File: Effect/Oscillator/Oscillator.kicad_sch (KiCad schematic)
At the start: 19 parts, among them J1 Conn_01x04_Pin, J2 Conn_01x03_Pin, Q1 DMMT5401, Q2 DMMT5551, U1 OPA1655, U2 LM393

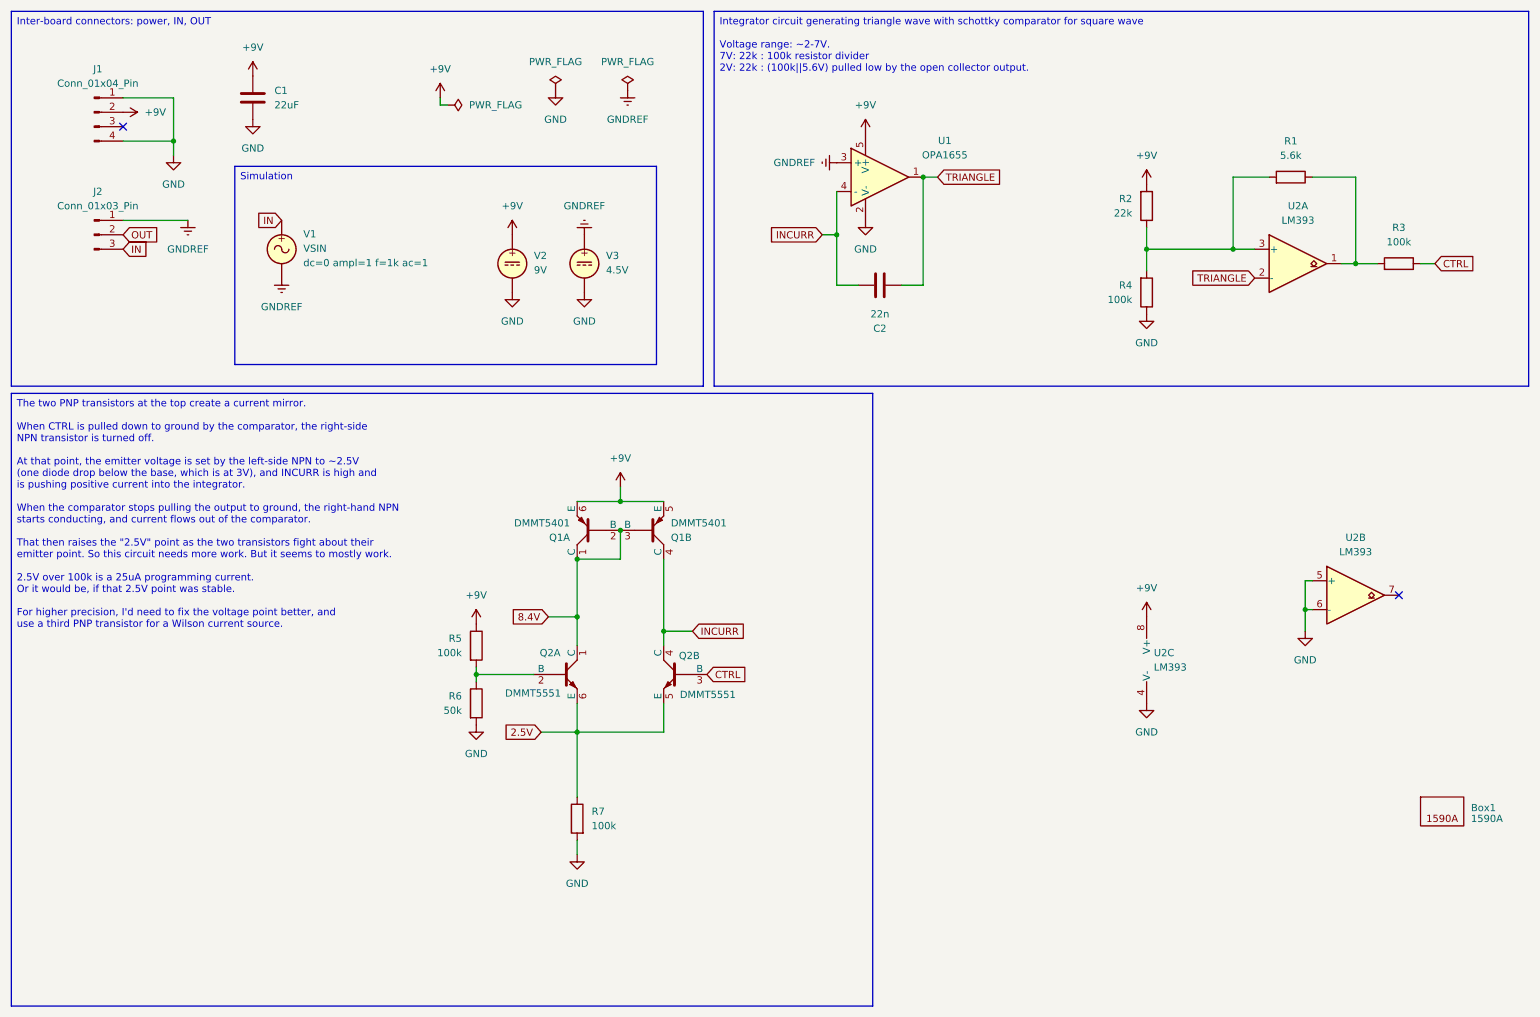
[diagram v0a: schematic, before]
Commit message: Connect up oscillator into a test board
Make a 'sineish' output by using a dual opamp and another integrator
circuit to turn the triangle wave into something that approximates a
sine wave.

It would be closer if my triangle wave was more balanced, but it looks
reasonable.  Even if the volume ends up being frequency dependent
because of how the integrator works - I haven't figured out how to fix
that part up.

Now it's an "effects pedal" with no inputs, only an output.  Simplest
way to test it.

Signed-off-by: Linus Torvalds <torvalds@linux-foundation.org>
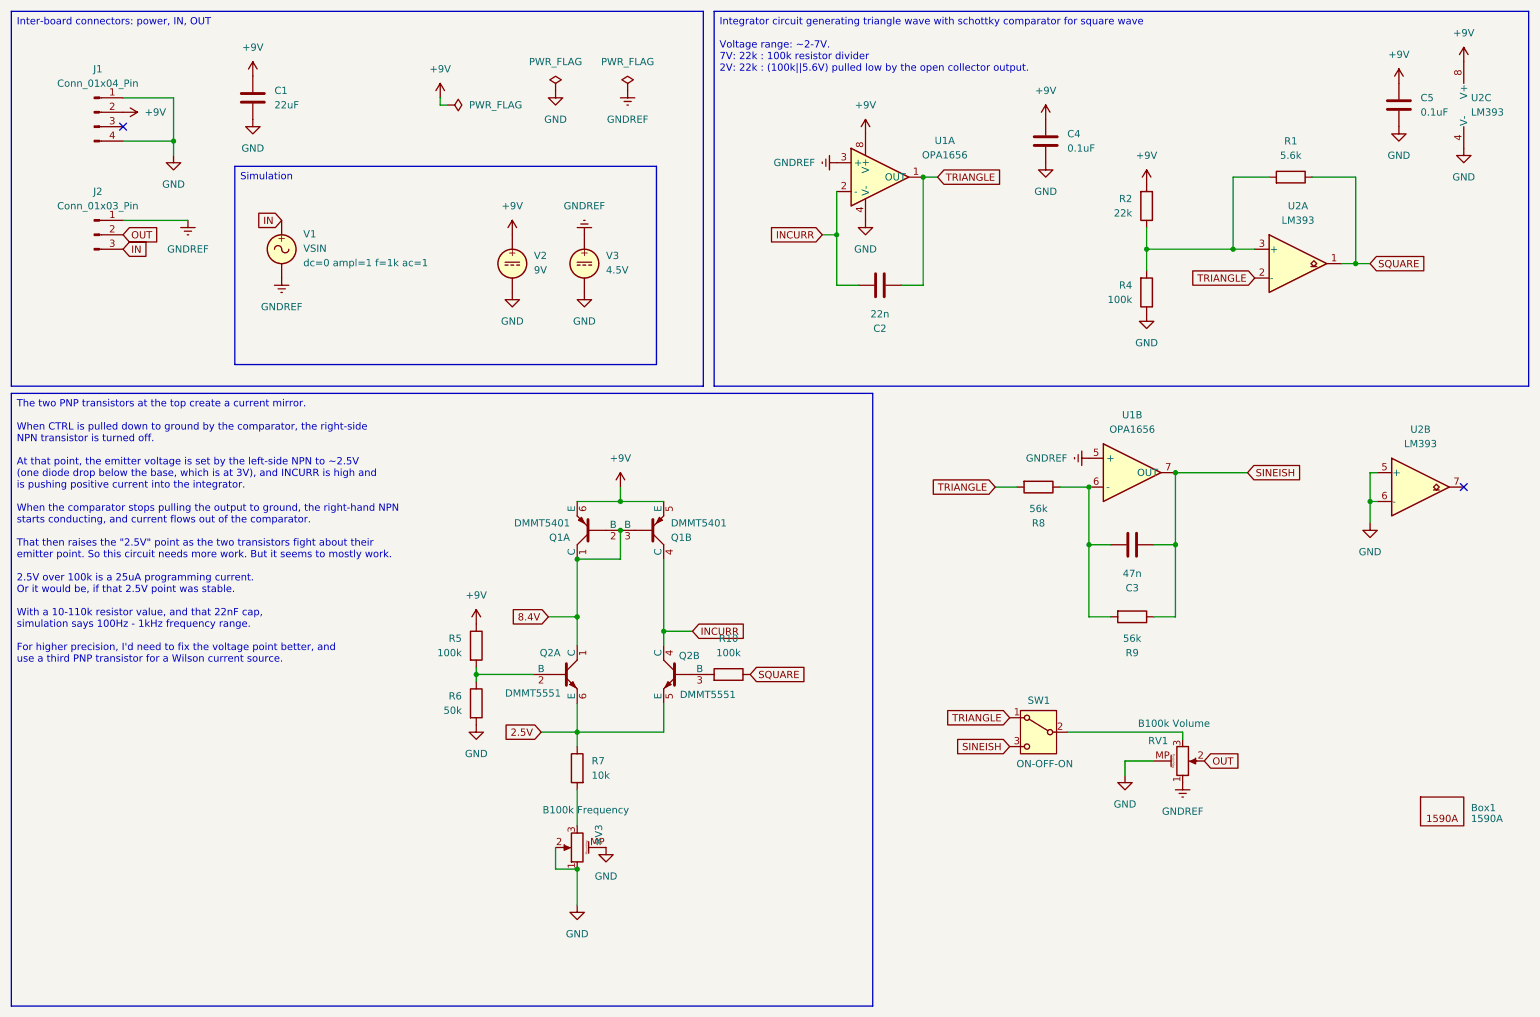
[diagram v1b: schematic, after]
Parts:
- removed R3: 100k, Resistor_SMD:R_0805_2012Metric, symbol Device:R
- removed U1: OPA1655, Package_TO_SOT_SMD:SOT-23-5, symbol Mylib:OPA1655DVB
- added C3: 47n, Capacitor_SMD:C_1206_3216Metric, symbol Device:C
- added C4, C5: 0.1uF, Mylib:C_0704_1810Metric, symbol Device:C
- added R10: 100k, Resistor_SMD:R_0805_2012Metric, symbol Device:R
- added R8, R9: 56k, Resistor_SMD:R_0805_2012Metric, symbol Device:R
- added RV1: B100k Volume, Mylib:Potentiometer_9mm_MP, symbol Device:R_Potentiometer_MountingPin
- added RV3: B100k Frequency, Mylib:Potentiometer_9mm_MP, symbol Device:R_Potentiometer_MountingPin
- added SW1: ON-OFF-ON, Connector_PinHeader_2.54mm:PinHeader_1x03_P2.54mm_Vertical, symbol Switch:SW_SPDT
- added U1: OPA1656, Package_SO:SOIC-8_3.9x4.9mm_P1.27mm, symbol Mylib:OPA1656
- R7: value 100k -> 10k
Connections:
- net +9V: now also C4.1, C5.1, U1.8 (V+)
- net GND: now also C4.2, C5.2, RV1.MP (MountPin), RV3.1, RV3.2, RV3.MP (MountPin), U1.4 (V-); no longer R7.2
- net GNDREF: now also RV1.1, U1.3 (+), U1.5 (+)
- net INCURR: now also U1.2 (-)
- net OUT: now also RV1.2
- net TRIANGLE: now also R8.2, SW1.1 (A), U1.1 (OUT)
- net SQUARE: now reaches R1.1, U2.1
- net SQUARE: now also R10.1
- net CTRL: no longer names the net of Q2.3 (B)
- net CTRL: now also R10.2
- new net: C3.1, R8.1, R9.2, U1.6 (-)
- new net: R7.2, RV3.3
- new net: RV1.3, SW1.2 (B)
- new net SINEISH: C3.2, R9.1, SW1.3 (C), U1.7 (OUT)
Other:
- moved on the sheet: R7, U2B, U2C

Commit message: Fix up component size on oscillator board
When actually receiving the boards and starting to build them up, I
noticed that I made a couple of the small caps be 1206 sized.  I do have
those, but my standard size for the nF caps is 0805, and that's what all
my small C0G caps are.

So fix it up for if I ever re-use this.

Signed-off-by: Linus Torvalds <torvalds@linux-foundation.org>
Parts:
- C2, C3: footprint Capacitor_SMD:C_1206_3216Metric -> Capacitor_SMD:C_0805_2012Metric
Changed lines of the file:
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@@
 			)
 		)
-		(property "Footprint" "Capacitor_SMD:C_1206_3216Metric"
+		(property "Footprint" "Capacitor_SMD:C_0805_2012Metric"
 			(at 215.9 110.1852 0)
 			(effects
@@
 			)
 		)
-		(property "Footprint" "Capacitor_SMD:C_1206_3216Metric"
+		(property "Footprint" "Capacitor_SMD:C_0805_2012Metric"
 			(at 171.45 64.4652 0)
 			(effects

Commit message: More footprint updates: avoid MSOP-8
Ok, so I intentionally got the comparator in both SOIC-8 and MSOP-8 to
see if the MSOP-8 is usable.

And sure, I can still solder them by hand, but it's another case of
"that's no fun".  So chalk it up as another learning experience, and
just go for SOIC-8.

I think I should just stick to 1.27mm lead spacing in general, although
SOT-23-6 is still ok and doesn't make me go "no fun" at 0.95mm.

But I think MSOP - whether 0.65mm or 0.5mm lead spacing - is for
machines.

Signed-off-by: Linus Torvalds <torvalds@linux-foundation.org>
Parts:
- U2: footprint Package_SO:MSOP-8_3x3mm_P0.65mm -> Package_SO:SOIC-8_3.9x4.9mm_P1.27mm
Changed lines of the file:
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@@
 			)
 		)
-		(property "Footprint" "Package_SO:MSOP-8_3x3mm_P0.65mm"
+		(property "Footprint" "Package_SO:SOIC-8_3.9x4.9mm_P1.27mm"
 			(at 262.89 99.06 0)
 			(effects
@@
 			)
 		)
-		(property "Footprint" "Package_SO:MSOP-8_3x3mm_P0.65mm"
+		(property "Footprint" "Package_SO:SOIC-8_3.9x4.9mm_P1.27mm"
 			(at 241.3 59.69 0)
 			(effects
@@
 			)
 		)
-		(property "Footprint" "Package_SO:MSOP-8_3x3mm_P0.65mm"
+		(property "Footprint" "Package_SO:SOIC-8_3.9x4.9mm_P1.27mm"
 			(at 273.05 31.75 0)
 			(effects
